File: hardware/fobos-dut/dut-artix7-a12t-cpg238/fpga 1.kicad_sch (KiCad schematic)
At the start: 24 parts

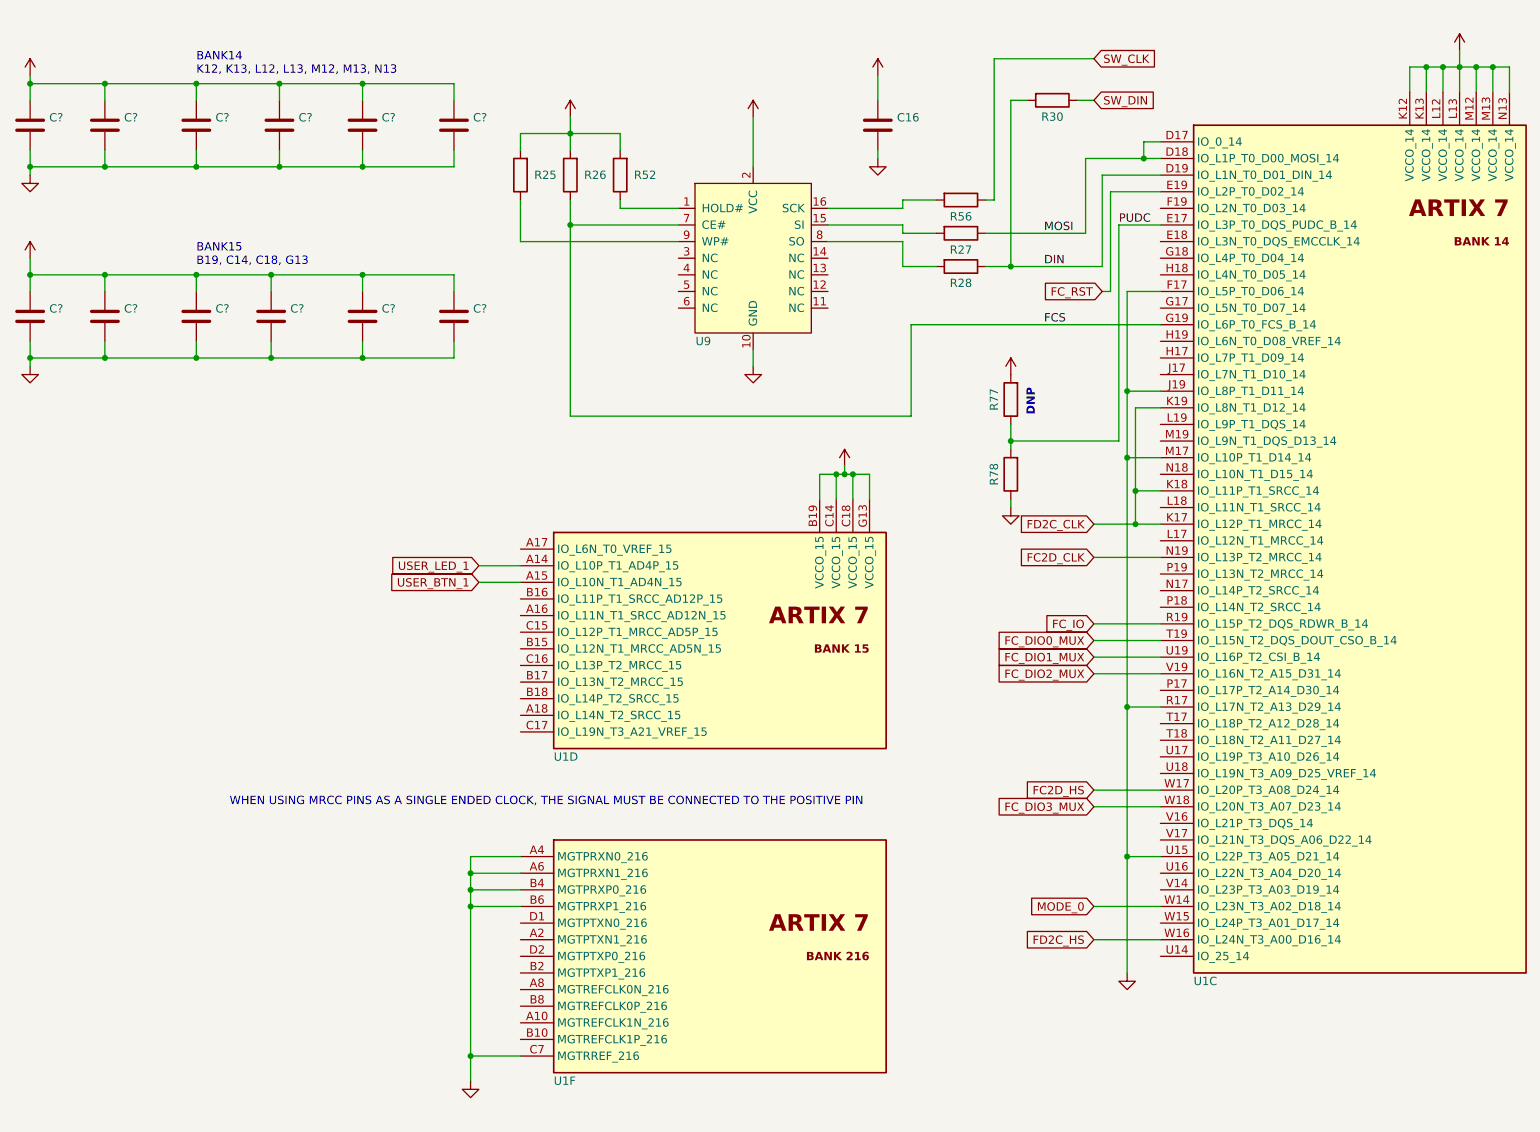
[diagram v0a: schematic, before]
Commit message: transitioned artix-7 dut to Kikad 6
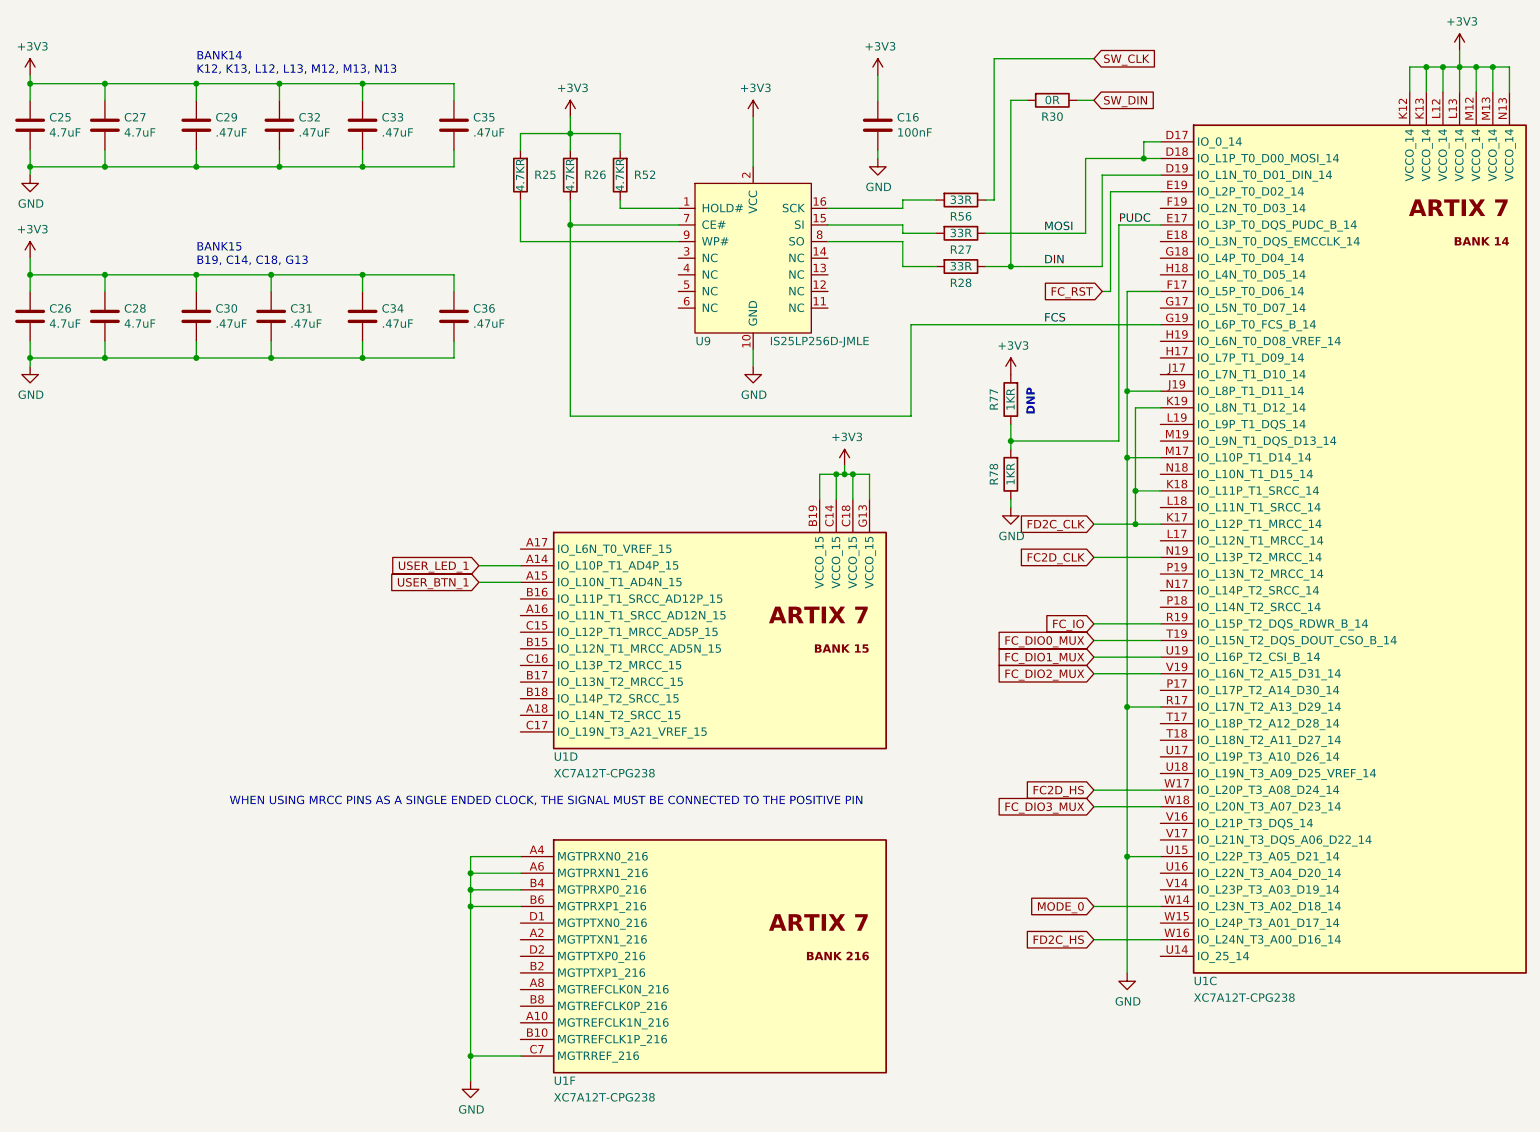
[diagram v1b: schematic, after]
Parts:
- C16: value (none) -> 100nF; footprint (none) -> Capacitor_SMD:C_0603_1608Metric
- C25, C26, C27, C28: renamed from C?; value (none) -> 4.7uF; footprint (none) -> Capacitor_SMD:C_0402_1005Metric_Pad0.74x0.62mm_HandSolder
- C29, C30, C31, C32, C33, C34, C35, C36: renamed from C?; value (none) -> .47uF; footprint (none) -> Capacitor_SMD:C_0402_1005Metric_Pad0.74x0.62mm_HandSolder
- R25, R26, R52: value (none) -> 4.7KR; footprint (none) -> Resistor_SMD:R_0603_1608Metric
- R27, R28, R56: value (none) -> 33R; footprint (none) -> Resistor_SMD:R_0603_1608Metric
- R30: value (none) -> 0R; footprint (none) -> Resistor_SMD:R_0603_1608Metric
- R77, R78: value (none) -> 1KR; footprint (none) -> Resistor_SMD:R_0603_1608Metric
- U1: value (none) -> XC7A12T-CPG238; footprint (none) -> Package_BGA:Xilinx_CPG238
- U9: value (none) -> IS25LP256D-JMLE; footprint (none) -> Package_SO:SOIC-16W_7.5x10.3mm_P1.27mm
